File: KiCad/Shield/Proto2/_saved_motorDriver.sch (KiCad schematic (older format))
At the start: 8 parts, among them J2 CONN_01X04, U2 L298_TH

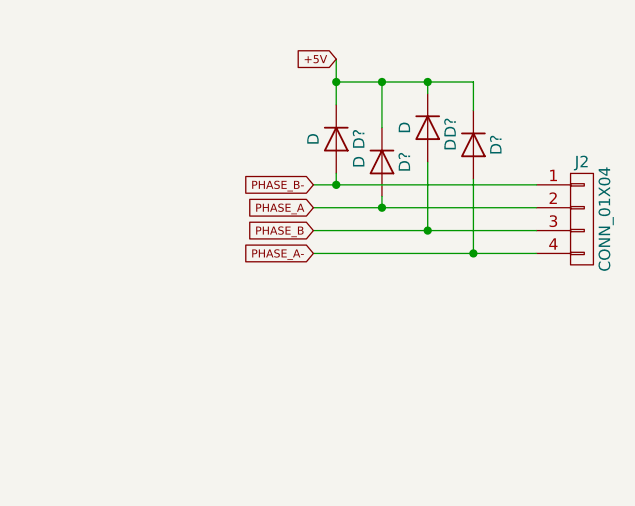
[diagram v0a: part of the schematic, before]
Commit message: added clearing graphic to gui
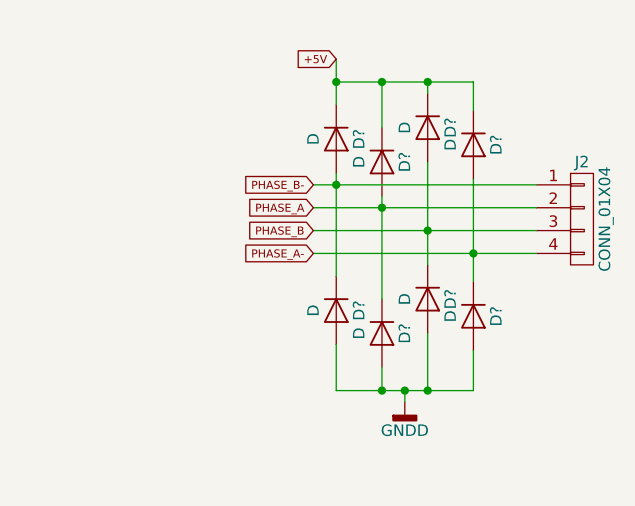
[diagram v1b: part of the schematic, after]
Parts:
- added D? (x4): D, Diodes_THT:D_T-1_P10.16mm_Horizontal, symbol D
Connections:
- net GNDD: now also D?.2 (A), D?.2 (A), D?.2 (A), D?.2 (A)
- net PHASE_A: now also D?.1 (K)
- net PHASE_A-: now also D?.1 (K)
- net PHASE_B: now also D?.1 (K)
- net PHASE_B-: now also D?.1 (K)
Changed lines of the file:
@@
 Connection ~ 5850 3600
 Wire Wire Line
-	7925 2850 7925 2800
+	7925 2800 7925 3250
 Wire Wire Line
-	8125 2650 8125 2950
+	8125 2650 8125 3100
 Wire Wire Line
-	8325 2725 8325 3050
+	8325 2725 8325 3175
 Connection ~ 8325 3050
 Connection ~ 8125 2950
@@
 Connection ~ 7925 2300
 Wire Wire Line
-	7725 2700 7725 2750
+	7725 2700 7725 3150
 Wire Wire Line
 	7625 2750 8600 2750
@@
 Text GLabel 7725 2200 0    35   Input ~ 0
 +5V
+$Comp
+L D D?
+U 1 1 5AD318C8
+P 7725 3300
+F 0 "D?" H 7725 3400 50  0000 C CNN
+F 1 "D" H 7725 3200 50  0000 C CNN
+F 2 "Diodes_THT:D_T-1_P10.16mm_Horizontal" H 7725 3300 50  0001 C CNN
+F 3 "" H 7725 3300 50  0001 C CNN
+	1    7725 3300
+	0    1    1    0
+$EndComp
+$Comp
+L D D?
+U 1 1 5AD318CE
+P 7925 3400
+F 0 "D?" H 7925 3500 50  0000 C CNN
+F 1 "D" H 7925 3300 50  0000 C CNN
+F 2 "Diodes_THT:D_T-1_P10.16mm_Horizontal" H 7925 3400 50  0001 C CNN
+F 3 "" H 7925 3400 50  0001 C CNN
+	1    7925 3400
+	0    1    1    0
+$EndComp
+$Comp
+L D D?
+U 1 1 5AD318D4
+P 8125 3250
+F 0 "D?" H 8125 3350 50  0000 C CNN
+F 1 "D" H 8125 3150 50  0000 C CNN
+F 2 "Diodes_THT:D_T-1_P10.16mm_Horizontal" H 8125 3250 50  0001 C CNN
+F 3 "" H 8125 3250 50  0001 C CNN
+	1    8125 3250
+	0    1    1    0
+$EndComp
+$Comp
+L D D?
+U 1 1 5AD318DA
+P 8325 3325
+F 0 "D?" H 8325 3425 50  0000 C CNN
+F 1 "D" H 8325 3225 50  0000 C CNN
+F 2 "Diodes_THT:D_T-1_P10.16mm_Horizontal" H 8325 3325 50  0001 C CNN
+F 3 "" H 8325 3325 50  0001 C CNN
+	1    8325 3325
+	0    1    1    0
+$EndComp
+Wire Wire Line
+	7725 3450 7725 3650
+Wire Wire Line
+	7725 3650 8325 3650
+Wire Wire Line
+	8325 3650 8325 3475
+Wire Wire Line
+	8125 3400 8125 3650
+Connection ~ 8125 3650
+Wire Wire Line
+	7925 3550 7925 3650
+Connection ~ 7925 3650
+Wire Wire Line
+	8025 3650 8025 3700
+Connection ~ 8025 3650
+$Comp
+L GNDD #PWR?
+U 1 1 5AD31B41
+P 8025 3700
+F 0 "#PWR?" H 8025 3450 50  0001 C CNN
+F 1 "GNDD" H 8025 3575 50  0000 C CNN
+F 2 "" H 8025 3700 50  0001 C CNN
+F 3 "" H 8025 3700 50  0001 C CNN
+	1    8025 3700
+	1    0    0    -1
+$EndComp
 $EndSCHEMATC
